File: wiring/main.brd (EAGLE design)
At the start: 75.9 x 73.7 mm, 41 parts, among them IC1 attiny 2313A, J1 J7MM, J11 J7MM, J2 J5MM, J3 J10MM, J4 J7MM, J5 J5MM, J6 J5MM, Q1 12MHz, X1 USB-B

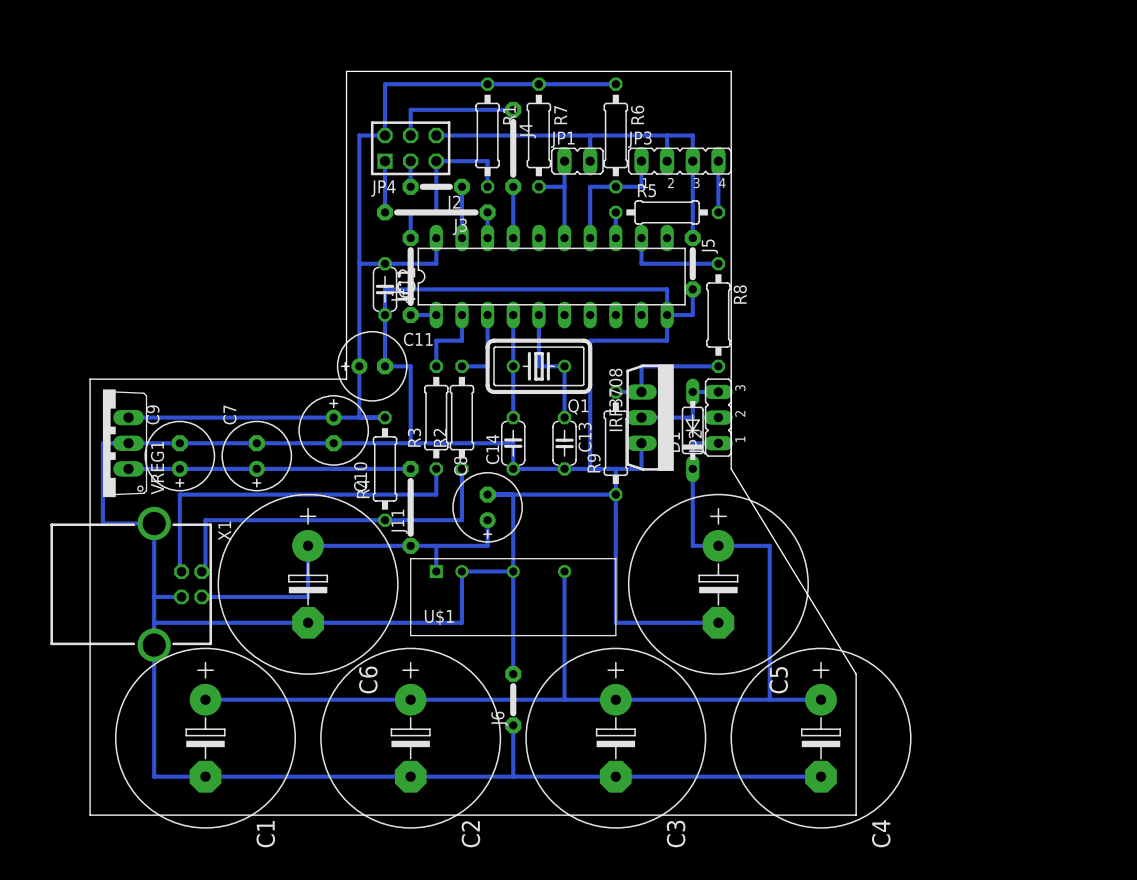
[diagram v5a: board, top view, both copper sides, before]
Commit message: wiring power led eingezeichnet
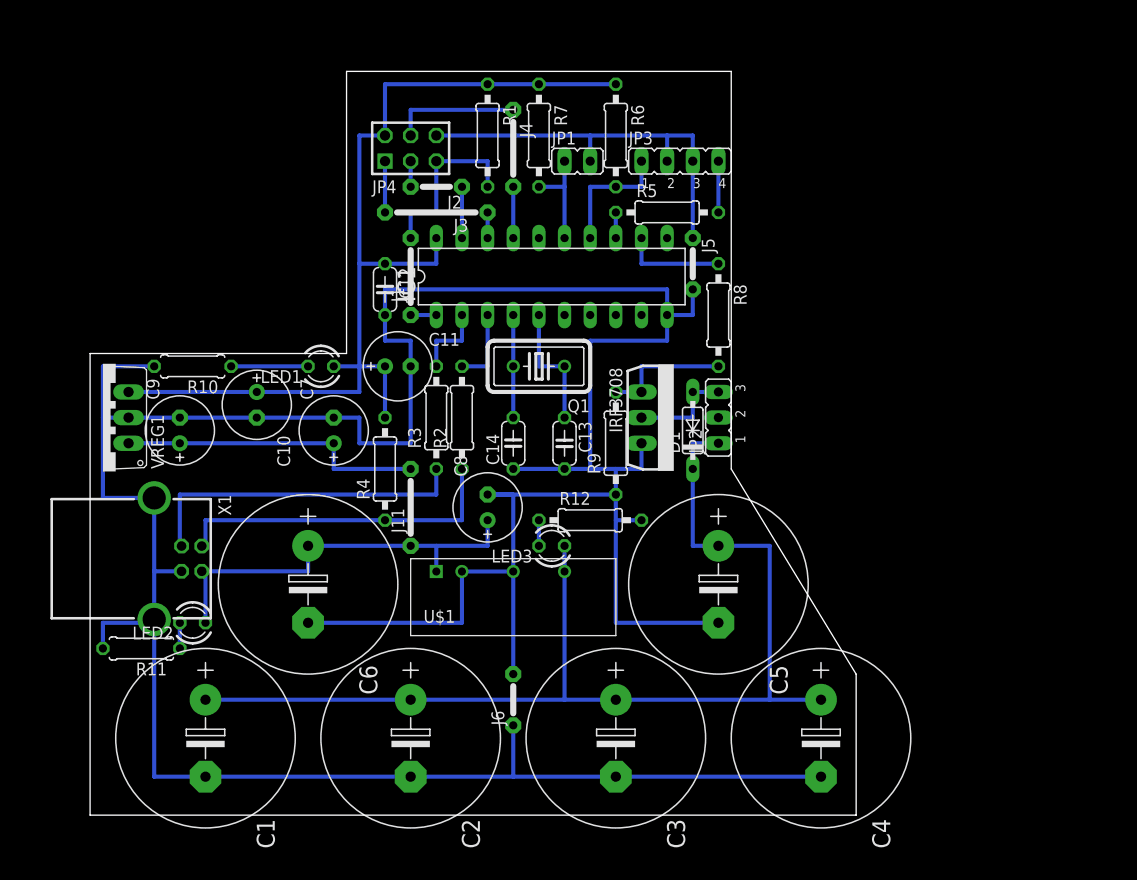
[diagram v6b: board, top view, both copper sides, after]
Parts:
- added LED1, LED2: (no value), led:LED3MM
- added LED3: LED 3MM 2MA GN, led:LED3MM
- added R10: 649, rcl:0207/7
- added R11: 1,5k, rcl:0207/7
- added R12: 6,49k, rcl:0207/10
- moved C10 8.03 mm to (17.8, 41.9)
- moved C7 8.03 mm to (25.4, 39.4)
- moved X1 2.54 mm to (7.62, 26.7)
- moved C11 2.54 mm to (31.8, 45.7)
- moved C9 2.54 mm to (10.2, 39.4)
- moved VREG1 2.54 mm to (2.54, 40.6)
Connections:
- removed net VCC: C10.+, C11.+, C12.1, IC1.20, JP4.2, R1.1, R4.2, R6.1, R7.1, VREG1.3
- new net +3V3: C10.+, C11.+, C12.1, IC1.20, JP4.2, LED1.A, R1.1, R4.2, R6.1, R7.1, VREG1.3
- new net N$1: LED3.K, R12.1
- new net N$4: LED2.K, R11.1
- new net N$5: LED1.K, R10.1
- net +15V: now also LED3.A
- net +5V: now also LED2.A
- net GND: now also R10.2, R11.2, R12.2
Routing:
- net +3V3: track 0.00 -> 99.1 mm
- net VCC: track 96.5 -> 0.00 mm
- net N$5: track 0.00 -> 7.62 mm
- net +5V: track 66.4 -> 71.9 mm
- net GND: track 386.3 -> 383.7 mm
- net +15V: track 109.2 -> 111.8 mm
- net N$4: track 0.00 -> 2.54 mm
- net N$1: track 0.00 -> 2.54 mm
- net D+: track 35.8 -> 33.2 mm
- net D-: track 35.9 -> 33.4 mm
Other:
- outline, holes or cut-outs redrawn

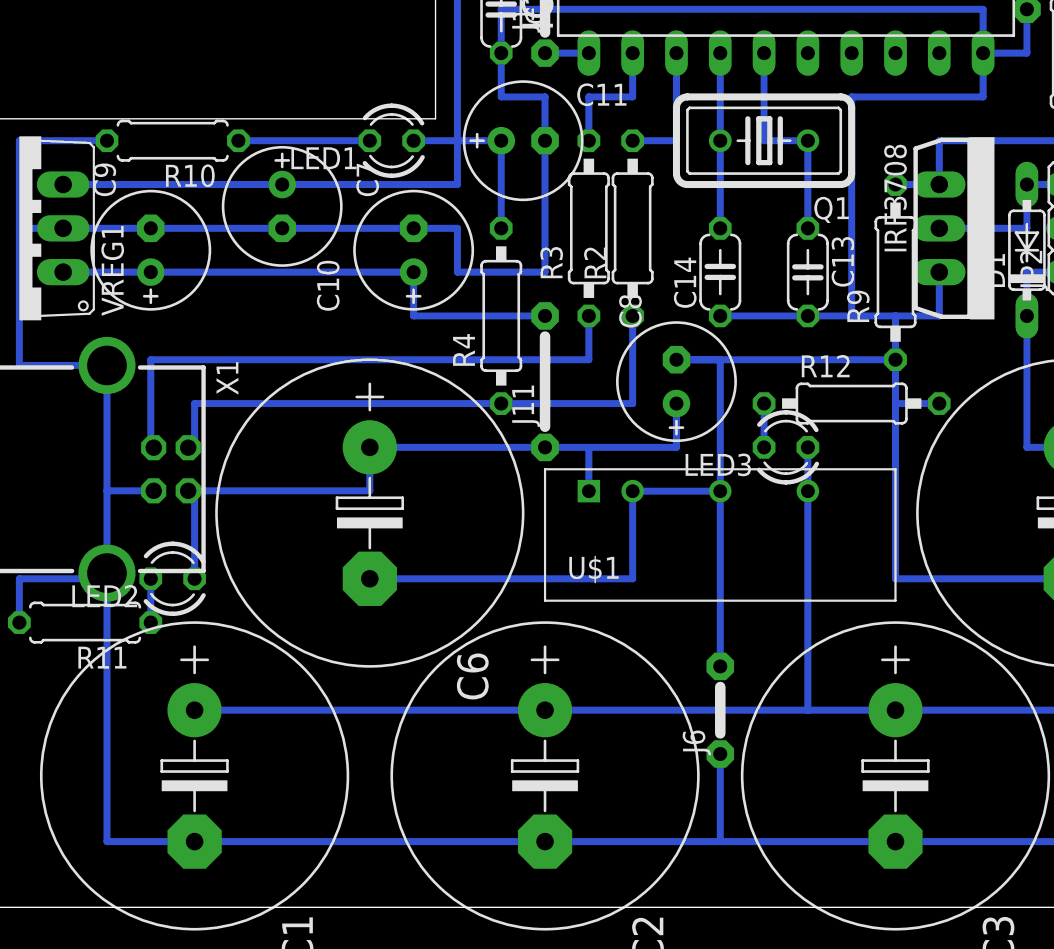
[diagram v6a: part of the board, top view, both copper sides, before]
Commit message: wiring schaltazeige led eingezeichnet
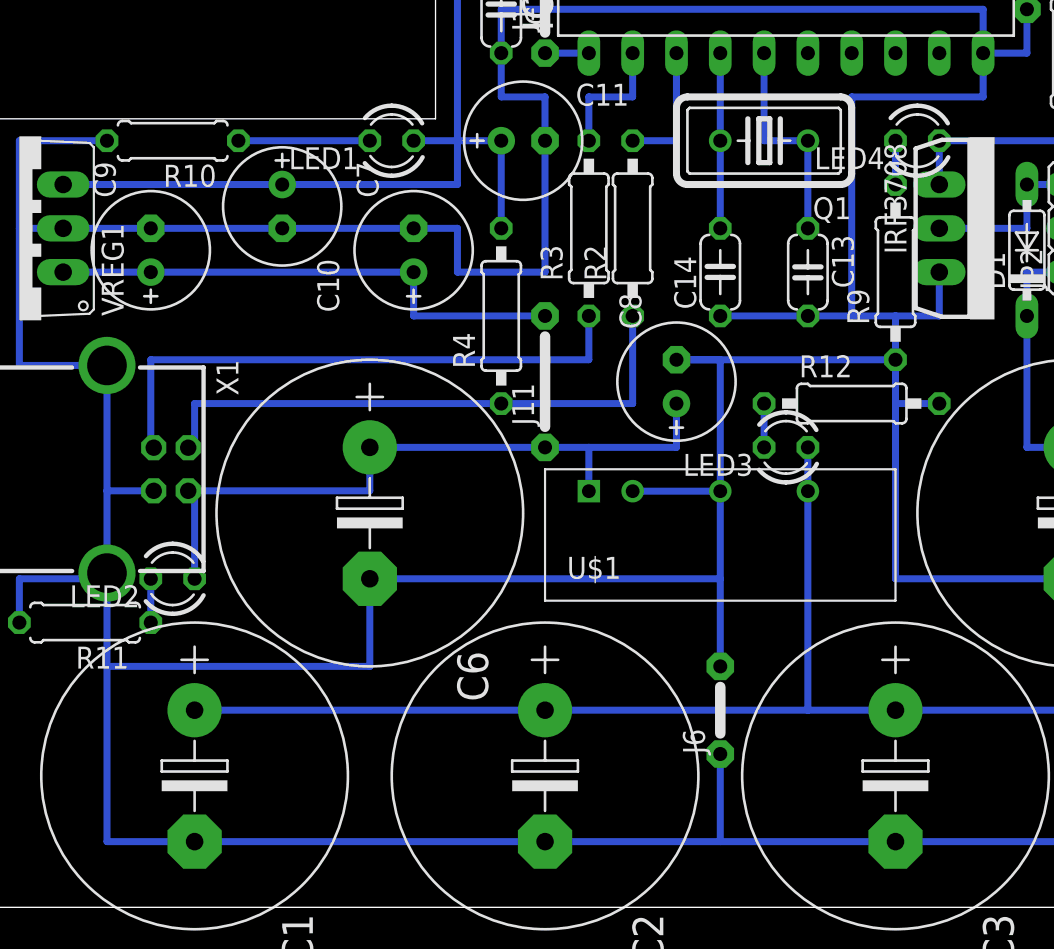
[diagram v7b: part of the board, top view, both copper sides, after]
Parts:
- added LED4: (no value), led:LED3MM
- R9: value 10k -> 549
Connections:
- new net N$6: LED4.K, R9.2
- net N$2: now also LED4.A; no longer R9.2
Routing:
- net GND: track 383.7 -> 404.0 mm
- net N$6: track 0.00 -> 2.54 mm
- net N$2: track 12.7 -> 10.2 mm
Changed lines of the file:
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@@
 <element name="D1" library="diode" package="DO35-7" value="1N4148DO35-7" x="60.96" y="39.37" rot="R90"/>
 <element name="IRF3708" library="transistor-power" package="TO262-V" value="IRF3704L-V" x="55.88" y="40.64" rot="R270"/>
-<element name="R9" library="rcl" package="0207/10" value="10k" x="53.34" y="38.1" rot="R90"/>
+<element name="R9" library="rcl" package="0207/10" value="549" x="53.34" y="38.1" rot="R90"/>
 <element name="C8" library="resistor" package="E2,5-7" value="220µ" x="40.64" y="31.75" rot="R90"/>
 <element name="U$1" library="eigene" package="SIL7" value="SIM2-0515S" x="35.56" y="25.4"/>
@@
 <element name="R11" library="rcl" package="0207/7" value="1,5k" x="6.35" y="17.78" rot="R180"/>
 <element name="R12" library="rcl" package="0207/10" value="6,49k" x="50.8" y="30.48"/>
+<element name="LED4" library="led" package="LED3MM" value="" x="54.61" y="45.72" rot="R180"/>
 </elements>
 <signals>
 <signal name="N$2">
 <contactref element="R8" pad="2"/>
-<contactref element="R9" pad="2"/>
 <contactref element="IRF3708" pad="1"/>
 <wire x1="55.88" y1="43.18" x2="55.88" y2="45.72" width="0.4064" layer="16"/>
 <wire x1="55.88" y1="45.72" x2="63.5" y2="45.72" width="0.4064" layer="16"/>
-<wire x1="55.88" y1="43.18" x2="53.34" y2="43.18" width="0.4064" layer="16"/>
+<contactref element="LED4" pad="A"/>
+<wire x1="55.88" y1="45.72" x2="55.88" y2="43.18" width="0" layer="19" extent="1-1"/>
 </signal>
 <signal name="+5V">
@@
 <contactref element="IRF3708" pad="3"/>
 <contactref element="R9" pad="1"/>
-<wire x1="7.62" y1="20.32" x2="7.62" y2="5.08" width="0.4064" layer="16"/>
+<wire x1="7.62" y1="20.32" x2="7.62" y2="15.24" width="0.4064" layer="16"/>
+<wire x1="7.62" y1="15.24" x2="7.62" y2="5.08" width="0.4064" layer="16"/>
 <wire x1="53.34" y1="33.02" x2="53.34" y2="35.56" width="0.4064" layer="16"/>
 <wire x1="53.34" y1="35.56" x2="50.8" y2="35.56" width="0.4064" layer="16"/>
@@
 <wire x1="53.34" y1="30.48" x2="53.34" y2="33.02" width="0.4064" layer="16"/>
 <wire x1="40.64" y1="33.02" x2="53.34" y2="33.02" width="0.4064" layer="16"/>
-<wire x1="22.86" y1="20.32" x2="38.1" y2="20.32" width="0.4064" layer="16"/>
-<wire x1="38.1" y1="20.32" x2="38.1" y2="25.4" width="0.4064" layer="16"/>
 <wire x1="38.1" y1="25.4" x2="43.18" y2="25.4" width="0.4064" layer="16"/>
 <contactref element="J5" pad="1"/>
@@
 <wire x1="43.18" y1="5.08" x2="33.02" y2="5.08" width="0.4064" layer="16"/>
 <wire x1="53.34" y1="5.08" x2="43.18" y2="5.08" width="0.4064" layer="16"/>
-<wire x1="43.18" y1="15.24" x2="43.18" y2="33.02" width="0.4064" layer="16"/>
+<wire x1="43.18" y1="15.24" x2="43.18" y2="20.32" width="0.4064" layer="16"/>
+<wire x1="43.18" y1="20.32" x2="43.18" y2="33.02" width="0.4064" layer="16"/>
 <wire x1="43.18" y1="33.02" x2="40.64" y2="33.02" width="0.4064" layer="16"/>
 <wire x1="5.08" y1="40.64" x2="10.16" y2="40.64" width="0.4064" layer="16"/>
@@
 <wire x1="7.62" y1="45.72" x2="2.54" y2="45.72" width="0.4064" layer="16"/>
 <wire x1="2.54" y1="45.72" x2="2.54" y2="40.64" width="0.4064" layer="16"/>
+<wire x1="22.86" y1="20.32" x2="22.86" y2="15.24" width="0.4064" layer="16"/>
+<wire x1="22.86" y1="15.24" x2="7.62" y2="15.24" width="0.4064" layer="16"/>
 <wire x1="60.96" y1="53.34" x2="60.96" y2="58.42" width="0" layer="19" extent="1-1"/>
-<wire x1="38.1" y1="20.32" x2="43.18" y2="15.24" width="0" layer="19" extent="16-16"/>
+<wire x1="43.18" y1="25.4" x2="43.18" y2="33.02" width="0" layer="19" extent="16-16"/>
+<wire x1="22.86" y1="20.32" x2="43.18" y2="20.32" width="0.4064" layer="16"/>
 </signal>
 <signal name="SCK">
@@
 <wire x1="45.72" y1="73.66" x2="40.64" y2="73.66" width="0" layer="19" extent="1-1"/>
 </signal>
+<signal name="N$6">
+<contactref element="R9" pad="2"/>
+<contactref element="LED4" pad="K"/>
+<wire x1="53.34" y1="43.18" x2="53.34" y2="45.72" width="0.4064" layer="16"/>
+</signal>
 </signals>
